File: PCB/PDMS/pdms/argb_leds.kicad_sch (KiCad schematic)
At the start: 16 parts

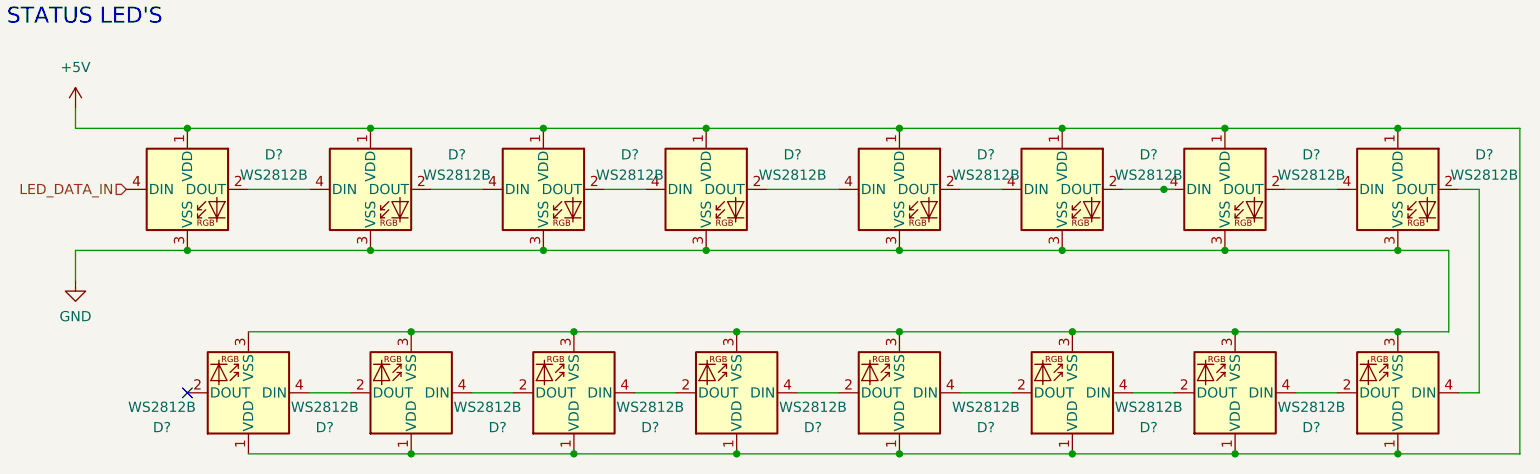
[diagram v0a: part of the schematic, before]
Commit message: Changed power section symbol library
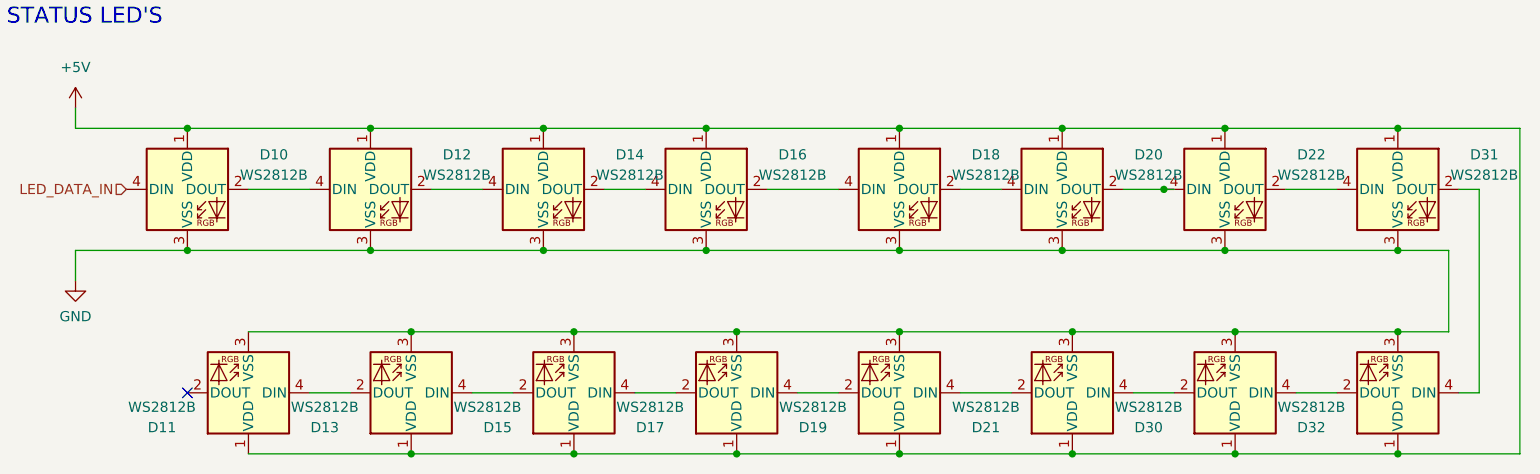
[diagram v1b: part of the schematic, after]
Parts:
- gave numbers to parts that had none: 16
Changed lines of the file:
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@@
   (symbol (lib_id "LED:WS2812B") (at 73.66 49.53 0) (unit 1)
     (in_bom yes) (on_board yes) (fields_autoplaced)
-    (property "Reference" "D?" (id 0) (at 84.455 45.1993 0))
+    (property "Reference" "D12" (id 0) (at 84.455 45.1993 0))
     (property "Value" "WS2812B" (id 1) (at 84.455 47.7393 0))
     (property "Footprint" "LED_SMD:LED_WS2812B-2020_PLCC4_2.0x2.0mm" (id 2) (at 74.93 57.15 0)
@@
   (symbol (lib_id "LED:WS2812B") (at 99.06 74.93 180) (unit 1)
     (in_bom yes) (on_board yes)
-    (property "Reference" "D?" (id 0) (at 89.535 79.2607 0))
+    (property "Reference" "D15" (id 0) (at 89.535 79.2607 0))
     (property "Value" "WS2812B" (id 1) (at 88.265 76.7207 0))
     (property "Footprint" "LED_SMD:LED_WS2812B-2020_PLCC4_2.0x2.0mm" (id 2) (at 97.79 67.31 0)
@@
   (symbol (lib_id "LED:WS2812B") (at 161.29 74.93 180) (unit 1)
     (in_bom yes) (on_board yes) (fields_autoplaced)
-    (property "Reference" "D?" (id 0) (at 150.495 79.2607 0))
+    (property "Reference" "D21" (id 0) (at 150.495 79.2607 0))
     (property "Value" "WS2812B" (id 1) (at 150.495 76.7207 0))
     (property "Footprint" "LED_SMD:LED_WS2812B-2020_PLCC4_2.0x2.0mm" (id 2) (at 160.02 67.31 0)
@@
   (symbol (lib_id "LED:WS2812B") (at 95.25 49.53 0) (unit 1)
     (in_bom yes) (on_board yes) (fields_autoplaced)
-    (property "Reference" "D?" (id 0) (at 106.045 45.1993 0))
+    (property "Reference" "D14" (id 0) (at 106.045 45.1993 0))
     (property "Value" "WS2812B" (id 1) (at 106.045 47.7393 0))
     (property "Footprint" "LED_SMD:LED_WS2812B-2020_PLCC4_2.0x2.0mm" (id 2) (at 96.52 57.15 0)
@@
   (symbol (lib_id "LED:WS2812B") (at 78.74 74.93 180) (unit 1)
     (in_bom yes) (on_board yes) (fields_autoplaced)
-    (property "Reference" "D?" (id 0) (at 67.945 79.2607 0))
+    (property "Reference" "D13" (id 0) (at 67.945 79.2607 0))
     (property "Value" "WS2812B" (id 1) (at 67.945 76.7207 0))
     (property "Footprint" "LED_SMD:LED_WS2812B-2020_PLCC4_2.0x2.0mm" (id 2) (at 77.47 67.31 0)
@@
   (symbol (lib_id "LED:WS2812B") (at 201.93 49.53 0) (unit 1)
     (in_bom yes) (on_board yes) (fields_autoplaced)
-    (property "Reference" "D?" (id 0) (at 212.725 45.1993 0))
+    (property "Reference" "D31" (id 0) (at 212.725 45.1993 0))
     (property "Value" "WS2812B" (id 1) (at 212.725 47.7393 0))
     (property "Footprint" "LED_SMD:LED_WS2812B-2020_PLCC4_2.0x2.0mm" (id 2) (at 203.2 57.15 0)
@@
   (symbol (lib_id "power:GND") (at 36.83 60.96 0) (unit 1)
     (in_bom yes) (on_board yes) (fields_autoplaced)
-    (property "Reference" "#PWR?" (id 0) (at 36.83 67.31 0)
+    (property "Reference" "#PWR0193" (id 0) (at 36.83 67.31 0)
       (effects (font (size 1.27 1.27)) hide)
     )
@@
   (symbol (lib_id "LED:WS2812B") (at 139.7 74.93 180) (unit 1)
     (in_bom yes) (on_board yes) (fields_autoplaced)
-    (property "Reference" "D?" (id 0) (at 128.905 79.2607 0))
+    (property "Reference" "D19" (id 0) (at 128.905 79.2607 0))
     (property "Value" "WS2812B" (id 1) (at 128.905 76.7207 0))
     (property "Footprint" "LED_SMD:LED_WS2812B-2020_PLCC4_2.0x2.0mm" (id 2) (at 138.43 67.31 0)
@@
   (symbol (lib_id "power:+5V") (at 36.83 39.37 0) (unit 1)
     (in_bom yes) (on_board yes) (fields_autoplaced)
-    (property "Reference" "#PWR?" (id 0) (at 36.83 43.18 0)
+    (property "Reference" "#PWR0198" (id 0) (at 36.83 43.18 0)
       (effects (font (size 1.27 1.27)) hide)
     )
@@
   (symbol (lib_id "LED:WS2812B") (at 58.42 74.93 180) (unit 1)
     (in_bom yes) (on_board yes) (fields_autoplaced)
-    (property "Reference" "D?" (id 0) (at 47.625 79.2607 0))
+    (property "Reference" "D11" (id 0) (at 47.625 79.2607 0))
     (property "Value" "WS2812B" (id 1) (at 47.625 76.7207 0))
     (property "Footprint" "LED_SMD:LED_WS2812B-2020_PLCC4_2.0x2.0mm" (id 2) (at 57.15 67.31 0)
@@
   (symbol (lib_id "LED:WS2812B") (at 115.57 49.53 0) (unit 1)
     (in_bom yes) (on_board yes) (fields_autoplaced)
-    (property "Reference" "D?" (id 0) (at 126.365 45.1993 0))
+    (property "Reference" "D16" (id 0) (at 126.365 45.1993 0))
     (property "Value" "WS2812B" (id 1) (at 126.365 47.7393 0))
     (property "Footprint" "LED_SMD:LED_WS2812B-2020_PLCC4_2.0x2.0mm" (id 2) (at 116.84 57.15 0)
@@
   (symbol (lib_id "LED:WS2812B") (at 180.34 49.53 0) (unit 1)
     (in_bom yes) (on_board yes) (fields_autoplaced)
-    (property "Reference" "D?" (id 0) (at 191.135 45.1993 0))
+    (property "Reference" "D22" (id 0) (at 191.135 45.1993 0))
     (property "Value" "WS2812B" (id 1) (at 191.135 47.7393 0))
     (property "Footprint" "LED_SMD:LED_WS2812B-2020_PLCC4_2.0x2.0mm" (id 2) (at 181.61 57.15 0)
@@
   (symbol (lib_id "LED:WS2812B") (at 139.7 49.53 0) (unit 1)
     (in_bom yes) (on_board yes) (fields_autoplaced)
-    (property "Reference" "D?" (id 0) (at 150.495 45.1993 0))
+    (property "Reference" "D18" (id 0) (at 150.495 45.1993 0))
     (property "Value" "WS2812B" (id 1) (at 150.495 47.7393 0))
     (property "Footprint" "LED_SMD:LED_WS2812B-2020_PLCC4_2.0x2.0mm" (id 2) (at 140.97 57.15 0)
@@
   (symbol (lib_id "LED:WS2812B") (at 160.02 49.53 0) (unit 1)
     (in_bom yes) (on_board yes) (fields_autoplaced)
-    (property "Reference" "D?" (id 0) (at 170.815 45.1993 0))
+    (property "Reference" "D20" (id 0) (at 170.815 45.1993 0))
     (property "Value" "WS2812B" (id 1) (at 170.815 47.7393 0))
     (property "Footprint" "LED_SMD:LED_WS2812B-2020_PLCC4_2.0x2.0mm" (id 2) (at 161.29 57.15 0)
@@
   (symbol (lib_id "LED:WS2812B") (at 119.38 74.93 180) (unit 1)
     (in_bom yes) (on_board yes) (fields_autoplaced)
-    (property "Reference" "D?" (id 0) (at 108.585 79.2607 0))
+    (property "Reference" "D17" (id 0) (at 108.585 79.2607 0))
     (property "Value" "WS2812B" (id 1) (at 108.585 76.7207 0))
     (property "Footprint" "LED_SMD:LED_WS2812B-2020_PLCC4_2.0x2.0mm" (id 2) (at 118.11 67.31 0)
@@
   (symbol (lib_id "LED:WS2812B") (at 50.8 49.53 0) (unit 1)
     (in_bom yes) (on_board yes) (fields_autoplaced)
-    (property "Reference" "D?" (id 0) (at 61.595 45.1993 0))
+    (property "Reference" "D10" (id 0) (at 61.595 45.1993 0))
     (property "Value" "WS2812B" (id 1) (at 61.595 47.7393 0))
     (property "Footprint" "LED_SMD:LED_WS2812B-2020_PLCC4_2.0x2.0mm" (id 2) (at 52.07 57.15 0)
@@
   (symbol (lib_id "LED:WS2812B") (at 201.93 74.93 180) (unit 1)
     (in_bom yes) (on_board yes) (fields_autoplaced)
-    (property "Reference" "D?" (id 0) (at 191.135 79.2607 0))
+    (property "Reference" "D32" (id 0) (at 191.135 79.2607 0))
     (property "Value" "WS2812B" (id 1) (at 191.135 76.7207 0))
     (property "Footprint" "LED_SMD:LED_WS2812B-2020_PLCC4_2.0x2.0mm" (id 2) (at 200.66 67.31 0)
@@
   (symbol (lib_id "LED:WS2812B") (at 181.61 74.93 180) (unit 1)
     (in_bom yes) (on_board yes) (fields_autoplaced)
-    (property "Reference" "D?" (id 0) (at 170.815 79.2607 0))
+    (property "Reference" "D30" (id 0) (at 170.815 79.2607 0))
     (property "Value" "WS2812B" (id 1) (at 170.815 76.7207 0))
     (property "Footprint" "LED_SMD:LED_WS2812B-2020_PLCC4_2.0x2.0mm" (id 2) (at 180.34 67.31 0)

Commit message: Final touch before PCB order
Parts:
- added D? (x2): WS2812B, LED_SMD:LED_WS2812B-2020_PLCC4_2.0x2.0mm, symbol LED:WS2812B
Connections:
- net +5V: now also D?.1 (VDD), D?.1 (VDD)
- net GND: now also D?.3 (VSS), D?.3 (VSS)
- net LED_DATA_IN: now also D?.4 (DIN); no longer D10.4 (DIN)
- new net: D10.4 (DIN), D?.2 (DOUT)
- new net: D?.2 (DOUT), D?.4 (DIN)
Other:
- moved on the sheet: D10, D11, D12, D13, D14, D15, D16, D17, D18, D19, D20, D21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

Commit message: Final touch PDMS
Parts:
- gave numbers to parts that had none: 2
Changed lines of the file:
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@@
   (symbol (lib_id "LED:WS2812B") (at 85.09 65.405 0) (unit 1)
     (in_bom yes) (on_board yes)
-    (property "Reference" "D?" (id 0) (at 95.885 61.0743 0))
+    (property "Reference" "D36" (id 0) (at 95.885 61.0743 0))
     (property "Value" "WS2812B" (id 1) (at 95.885 63.6143 0))
     (property "Footprint" "LED_SMD:LED_WS2812B-2020_PLCC4_2.0x2.0mm" (id 2) (at 86.36 73.025 0)
@@
   (symbol (lib_id "LED:WS2812B") (at 62.23 65.405 0) (unit 1)
     (in_bom yes) (on_board yes)
-    (property "Reference" "D?" (id 0) (at 73.025 61.0743 0))
+    (property "Reference" "D29" (id 0) (at 73.025 61.0743 0))
     (property "Value" "WS2812B" (id 1) (at 73.025 63.6143 0))
     (property "Footprint" "LED_SMD:LED_WS2812B-2020_PLCC4_2.0x2.0mm" (id 2) (at 63.5 73.025 0)

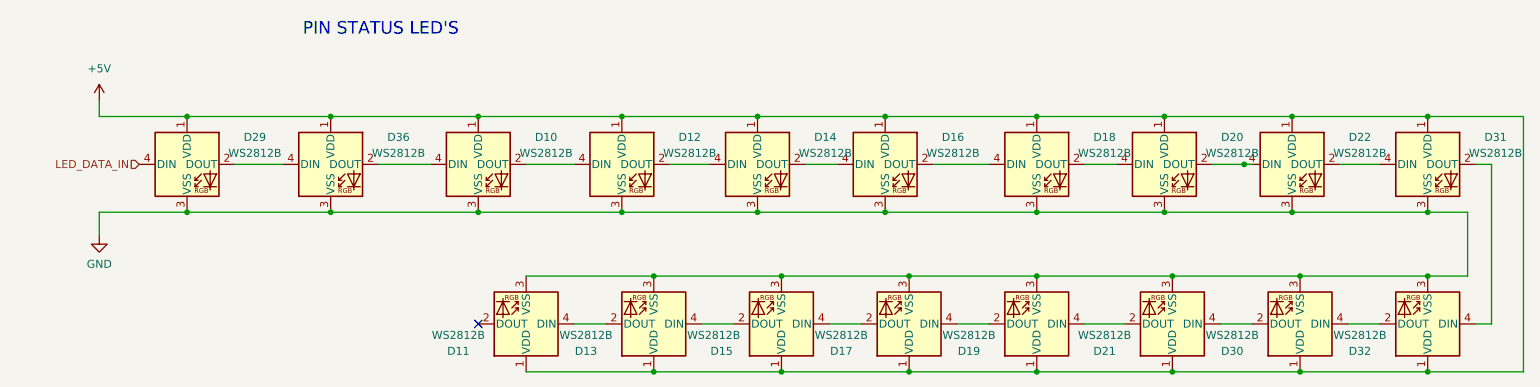
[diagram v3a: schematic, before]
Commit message: Changed main power connector, added USB-C, added BLE - not wired yet
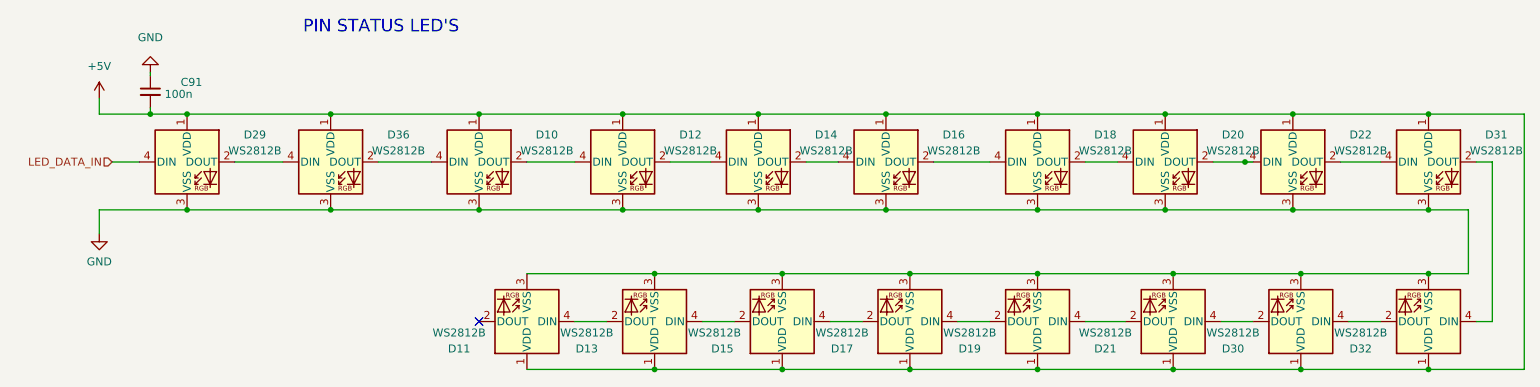
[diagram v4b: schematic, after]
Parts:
- added C91: 100n, Resistor_SMD:R_0402_1005Metric, symbol Device:C_Small
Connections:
- net +5V: now also C91.2
- net GND: now also C91.1

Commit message: Major changes with new switch
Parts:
- removed D10, D11, D12, D13, D14, D15, D16, D17, D18, D19, D20, D21, D22, D29, D30, D31, D32, D36: WS2812B, LED_SMD:LED_WS2812B-2020_PLCC4_2.0x2.0mm, symbol LED:WS2812B
- added D10, D11, D12, D13, D14, D15, D16, D17, D18, D19, D20, D21, D22, D29, D30, D31, D32, D36: WS2812B-2020, PDMS_Additional:WS2812B2020, symbol pdms_additional:WS2812B-2020
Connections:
- net +5V: now also D10.4 (VDD), D11.4 (VDD), D12.4 (VDD), D13.4 (VDD), D14.4 (VDD), D15.4 (VDD), D16.4 (VDD), D17.4 (VDD), D18.4 (VDD), D19.4 (VDD), D20.4 (VDD), D21.4 (VDD), D22.4 (VDD), D29.4 (VDD), D30.4 (VDD), D31.4 (VDD), D32.4 (VDD), D36.4 (VDD)
- net GND: now also D10.2 (GND), D11.2 (GND), D12.2 (GND), D13.2 (GND), D14.2 (GND), D15.2 (GND), D16.2 (GND), D17.2 (GND), D18.2 (GND), D19.2 (GND), D20.2 (GND), D21.2 (GND), D22.2 (GND), D29.2 (GND), D30.2 (GND), D31.2 (GND), D32.2 (GND), D36.2 (GND)
- net LED_DATA_IN: now also D10.3 (DI)
- new net: D29.3 (DI), D31.1 (DO)
- new net: D30.1 (DO), D31.3 (DI)
- new net: D11.1 (DO), D32.3 (DI)
- new net: D11.3 (DI), D13.1 (DO)
- new net: D22.1 (DO), D30.3 (DI)
- new net: D20.1 (DO), D22.3 (DI)
- new net: D32.1 (DO), D36.3 (DI)
- new net: D12.1 (DO), D14.3 (DI)
- new net: D10.1 (DO), D12.3 (DI)
- new net: D13.3 (DI), D15.1 (DO)
- new net: D15.3 (DI), D17.1 (DO)
- new net: D17.3 (DI), D19.1 (DO)
- new net: D19.3 (DI), D21.1 (DO)
- new net: D16.1 (DO), D18.3 (DI)
- new net: D14.1 (DO), D16.3 (DI)
- new net: D18.1 (DO), D20.3 (DI)
- new net: D21.3 (DI), D29.1 (DO)

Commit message: Clean-up of schematics
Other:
- note added: "ARGB - informing LED's"
- note removed: "PIN STATUS LED'S"
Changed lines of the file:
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@@
     (stroke (width 0) (type default) (color 0 0 0 0))
   )
-  (text "PIN STATUS LED'S" (at 20.574 43.688 0)
-    (effects (font (size 2 2)) (justify left bottom))
+  (text "ARGB - informing LED's" (at 187.071 191.008 0)
+    (effects (font (size 2 2) italic) (justify left bottom))
   )
   (hierarchical_label "LED_DATA_IN" (shape input) (at 29.718 60.198 180)

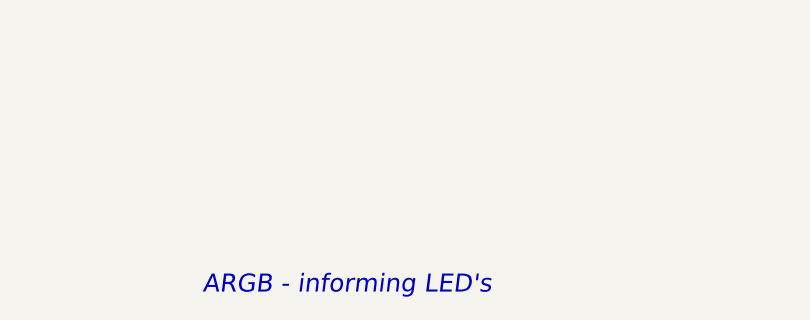
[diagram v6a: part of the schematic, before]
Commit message: WIP PCB folder structure and schematic clean-up
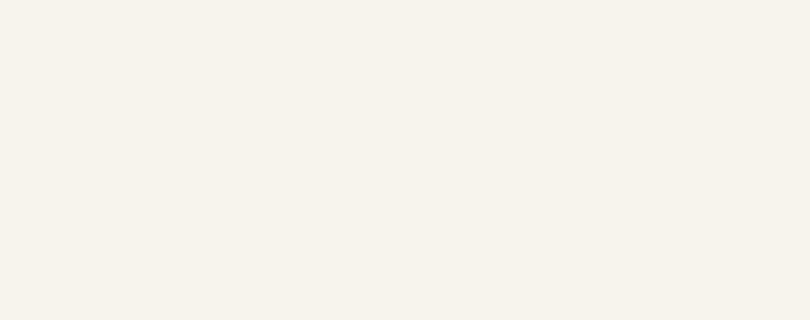
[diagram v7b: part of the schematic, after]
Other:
- note removed: "ARGB - informing LED's"
- company: (none) -> PGRacing Team
- title: (none) -> ARGB - notification LED's
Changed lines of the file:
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@@
 (kicad_sch (version 20211123) (generator eeschema)
   (paper "A4")
+  (title_block
+    (title "ARGB - notification LED's")
+    (rev "V4.2")
+    (company "PGRacing Team")
+    (comment 1 "Karol Pergoł")
+  )
   (junction (at 84.582 85.852) (diameter 0) (color 0 0 0 0)
   )
@@
     (stroke (width 0) (type default) (color 0 0 0 0))
   )
-  (text "ARGB - informing LED's" (at 187.071 191.008 0)
-    (effects (font (size 2 2) italic) (justify left bottom))
-  )
   (hierarchical_label "LED_DATA_IN" (shape input) (at 29.718 60.198 180)
